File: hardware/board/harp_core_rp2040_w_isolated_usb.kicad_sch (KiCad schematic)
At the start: 49 parts, among them J1 Conn_01x03_Male, J2 AudioJack3, J3 USB_C_Receptacle_USB2.0, U2 TPD2EUSB30, U3 ADUM4160, U4 RP2040, U5 W25Q16JVUXIQ, X1 ECS-TXO-2016

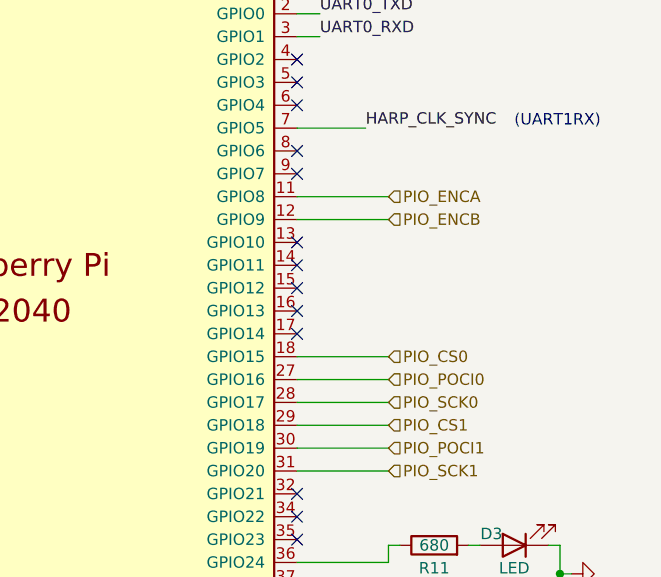
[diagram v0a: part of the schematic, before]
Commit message: update schematic
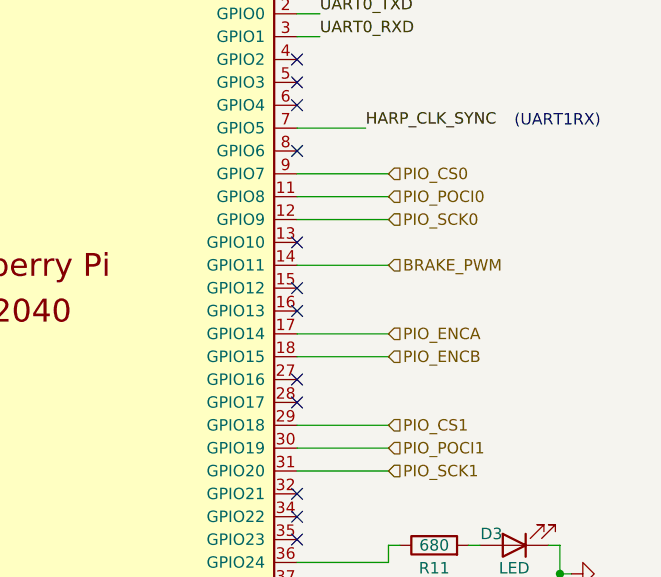
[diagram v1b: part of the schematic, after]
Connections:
- net PIO_CS0: now also U4.9 (GPIO7); no longer U4.18 (GPIO15)
- net PIO_ENCA: now also U4.17 (GPIO14); no longer U4.11 (GPIO8)
- net PIO_ENCB: now also U4.18 (GPIO15); no longer U4.12 (GPIO9)
- net PIO_POCI0: now also U4.11 (GPIO8); no longer U4.27 (GPIO16)
- net PIO_SCK0: now also U4.12 (GPIO9); no longer U4.28 (GPIO17)
- net BRAKE_PWM: now reaches U4.14 (GPIO11)
- no-connect marks 25 -> 24
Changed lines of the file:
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@@
   )
   (no_connect (at 244.475 144.78))
-  (no_connect (at 244.475 109.22))
   (no_connect (at 244.475 78.74))
-  (no_connect (at 244.475 101.6))
   (no_connect (at 244.475 147.32))
   (no_connect (at 244.475 132.08))
   (no_connect (at 244.475 81.28))
+  (no_connect (at 244.475 114.3))
   (no_connect (at 244.475 104.14))
   (no_connect (at 180.975 140.97))
@@
   (no_connect (at 180.975 114.3))
   (no_connect (at 244.475 83.82))
-  (no_connect (at 244.475 91.44))
   (no_connect (at 244.475 88.9))
   (no_connect (at 244.475 142.24))
+  (no_connect (at 244.475 99.06))
   (no_connect (at 244.475 106.68))
   (no_connect (at 42.545 52.07))
   (no_connect (at 29.845 105.41))
   (no_connect (at 139.065 109.22))
-  (no_connect (at 244.475 99.06))
+  (no_connect (at 244.475 116.84))
   (no_connect (at 244.475 149.86))
   (no_connect (at 244.475 129.54))
@@
     (stroke (width 0) (type default))
   )
-  (wire (pts (xy 244.475 111.76) (xy 254.635 111.76))
+  (wire (pts (xy 47.625 143.51) (xy 47.625 144.78))
     (stroke (width 0) (type default))
   )
-  (wire (pts (xy 47.625 143.51) (xy 47.625 144.78))
+  (wire (pts (xy 244.475 109.22) (xy 254.635 109.22))
     (stroke (width 0) (type default))
   )
@@
     (stroke (width 0) (type default))
   )
+  (wire (pts (xy 244.475 101.6) (xy 254.635 101.6))
+    (stroke (width 0) (type default))
+  )
   (wire (pts (xy 180.975 83.82) (xy 177.165 83.82))
     (stroke (width 0) (type default))
@@
     (stroke (width 0) (type default))
   )
-  (wire (pts (xy 244.475 114.3) (xy 254.635 114.3))
-    (stroke (width 0) (type default))
-  )
   (wire (pts (xy 244.475 119.38) (xy 254.635 119.38))
     (stroke (width 0) (type default))
@@
     (stroke (width 0) (type default))
   )
-  (wire (pts (xy 244.475 96.52) (xy 254.635 96.52))
+  (wire (pts (xy 244.475 93.98) (xy 254.635 93.98))
     (stroke (width 0) (type default))
   )
@@
     (stroke (width 0) (type default))
   )
-  (wire (pts (xy 244.475 93.98) (xy 254.635 93.98))
+  (wire (pts (xy 244.475 91.44) (xy 254.635 91.44))
     (stroke (width 0) (type default))
   )
@@
     (stroke (width 0) (type default))
   )
-  (wire (pts (xy 244.475 116.84) (xy 254.635 116.84))
-    (stroke (width 0) (type default))
-  )
   (wire (pts (xy 19.685 62.23) (xy 19.685 63.5))
     (stroke (width 0) (type default))
@@
     (stroke (width 0) (type default))
   )
+  (wire (pts (xy 244.475 111.76) (xy 254.635 111.76))
+    (stroke (width 0) (type default))
+  )
   (wire (pts (xy 19.685 63.5) (xy 27.305 63.5))
     (stroke (width 0) (type default))
@@
     (stroke (width 0) (type default))
   )
+  (wire (pts (xy 244.475 96.52) (xy 254.635 96.52))
+    (stroke (width 0) (type default))
+  )
   (wire (pts (xy 160.655 44.45) (xy 161.925 44.45))
     (stroke (width 0) (type default))
@@
     (effects (font (size 1.27 1.27)) (justify left))
   )
-  (hierarchical_label "PIO_POCI0" (shape input) (at 254.635 114.3 0) (fields_autoplaced)
+  (hierarchical_label "BRAKE_PWM" (shape input) (at 254.635 101.6 0) (fields_autoplaced)
+    (effects (font (size 1.27 1.27)) (justify left))
+  )
+  (hierarchical_label "PIO_POCI0" (shape input) (at 254.635 93.98 0) (fields_autoplaced)
     (effects (font (size 1.27 1.27)) (justify left))
   )
-  (hierarchical_label "PIO_SCK0" (shape input) (at 254.635 116.84 0) (fields_autoplaced)
+  (hierarchical_label "PIO_SCK0" (shape input) (at 254.635 96.52 0) (fields_autoplaced)
     (effects (font (size 1.27 1.27)) (justify left))
   )
-  (hierarchical_label "PIO_ENCA" (shape input) (at 254.635 93.98 0) (fields_autoplaced)
+  (hierarchical_label "PIO_ENCA" (shape input) (at 254.635 109.22 0) (fields_autoplaced)
     (effects (font (size 1.27 1.27)) (justify left))
   )
-  (hierarchical_label "PIO_ENCB" (shape input) (at 254.635 96.52 0) (fields_autoplaced)
+  (hierarchical_label "PIO_ENCB" (shape input) (at 254.635 111.76 0) (fields_autoplaced)
     (effects (font (size 1.27 1.27)) (justify left))
   )
-  (hierarchical_label "PIO_CS0" (shape input) (at 254.635 111.76 0) (fields_autoplaced)
+  (hierarchical_label "PIO_CS0" (shape input) (at 254.635 91.44 0) (fields_autoplaced)
     (effects (font (size 1.27 1.27)) (justify left))
   )

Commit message: update pcb
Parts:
- renumbered C2 to C1, C16 to C10, C17 to C11, C18 to C12, C19 to C13, C20 to C14, C21 to C15, C22 to C16, C23 to C17, C24 to C18, C25 to C19, C9 to C2, C11 to C3, C7 to C37, C8 to C4, C13 to C5, C5 to C56, C10 to C6, C12 to C7, C15 to C8, C14 to C9, D3 to D1, D4 to D2, D1 to D3, D2 to D4, J3 to J5, R9 to R10, R10 to R11, R8 to R9

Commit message: update sch and pcb
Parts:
- C11: Alternate CL21B106KOQNNNE -> GRM21BR61H106KE43L; Link https://www.digikey.com/en/products/detail/murata-electronics/GRM21BZ71E106KE15L/13904911 -> https://www.digikey.com/en/products/detail/murata-electronics/GRM21BR61H106KE43L/10326316; Manufacturer Number GRM21BZ71E106KE15L -> GRM21BR61H106KE43L; Rated Voltage 25V -> 50V; Temperature Coefficient X7R -> X5R; Tolerance (none) -> 10%
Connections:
- net BRAKE_PWM: now also U4.16 (GPIO13); no longer U4.14 (GPIO11)
- net PIO_CS0: now also U4.12 (GPIO9); no longer U4.9 (GPIO7)
- net PIO_ENCA: now also U4.27 (GPIO16); no longer U4.17 (GPIO14)
- net PIO_ENCB: now also U4.28 (GPIO17); no longer U4.18 (GPIO15)
- net PIO_POCI0: now also U4.13 (GPIO10); no longer U4.11 (GPIO8)
- net PIO_SCK0: now also U4.14 (GPIO11); no longer U4.12 (GPIO9)
- no-connect marks 24 -> 20

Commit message: update schematic; continue pcb draft
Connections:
- net BRAKE_PWM: now also U4.35 (GPIO23); no longer U4.16 (GPIO13)
- no-connect marks 20 -> 19
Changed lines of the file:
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@@
   (no_connect (at 244.602 78.74))
   (no_connect (at 244.602 147.32))
-  (no_connect (at 244.602 132.08))
   (no_connect (at 244.602 81.28))
   (no_connect (at 244.602 104.14))
@@
     (stroke (width 0) (type default))
   )
+  (wire (pts (xy 250.698 132.08) (xy 250.698 128.016))
+    (stroke (width 0) (type default))
+  )
   (wire (pts (xy 24.892 106.68) (xy 24.892 107.95))
     (stroke (width 0) (type default))
@@
     (stroke (width 0) (type default))
   )
-  (wire (pts (xy 244.602 106.68) (xy 254.762 106.68))
+  (wire (pts (xy 250.698 128.016) (xy 254.762 128.016))
     (stroke (width 0) (type default))
   )
@@
     (stroke (width 0) (type default))
   )
+  (wire (pts (xy 244.602 132.08) (xy 250.698 132.08))
+    (stroke (width 0) (type default))
+  )
   (wire (pts (xy 149.352 44.45) (xy 153.162 44.45))
     (stroke (width 0) (type default))
@@
     (effects (font (size 1.27 1.27)) (justify left))
   )
-  (hierarchical_label "BRAKE_PWM" (shape input) (at 254.762 106.68 0) (fields_autoplaced)
+  (hierarchical_label "BRAKE_PWM" (shape input) (at 254.762 128.016 0) (fields_autoplaced)
     (effects (font (size 1.27 1.27)) (justify left))
   )

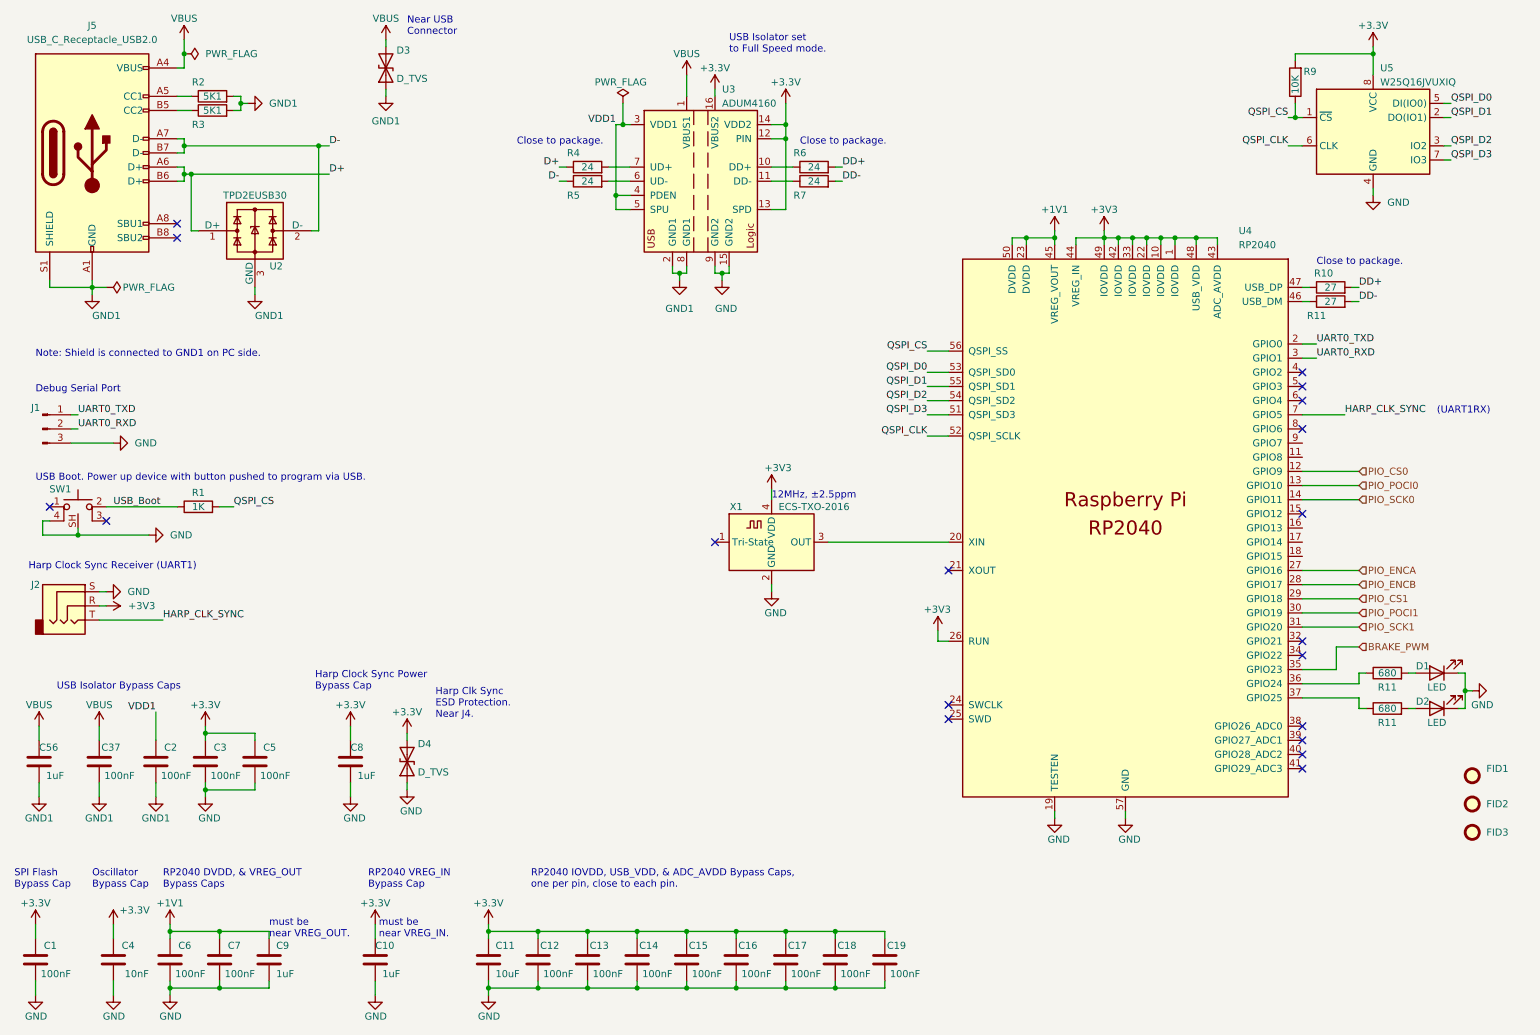
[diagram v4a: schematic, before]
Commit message: draft layout with analog brake driver circuit
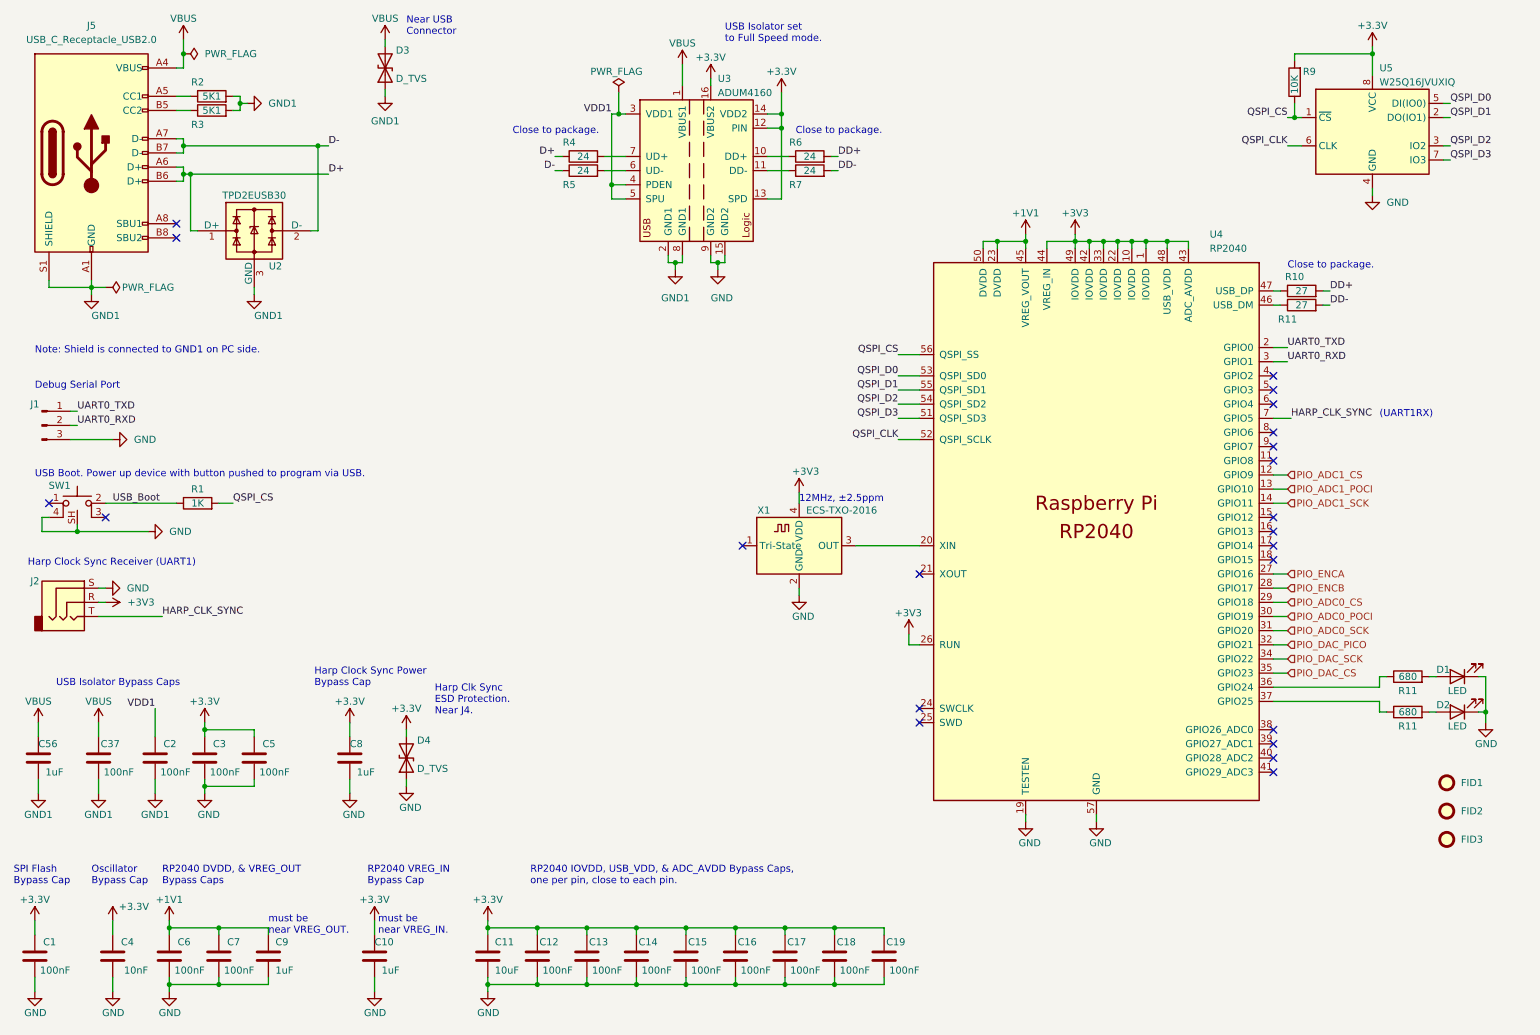
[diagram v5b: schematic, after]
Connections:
- net PIO_DAC_PICO: now reaches U4.32 (GPIO21)
- net PIO_DAC_SCK: now reaches U4.34 (GPIO22)
- net BRAKE_PWM renamed PIO_DAC_CS
- net PIO_CS0 renamed PIO_ADC1_CS
- net PIO_CS1 renamed PIO_ADC0_CS
- net PIO_POCI0 renamed PIO_ADC1_POCI
- net PIO_POCI1 renamed PIO_ADC0_POCI
- net PIO_SCK0 renamed PIO_ADC1_SCK
- net PIO_SCK1 renamed PIO_ADC0_SCK
- no-connect marks 19 -> 22
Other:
- moved on the sheet: C1, C10, C11, C12, C13, C14, C15, C16, C17, C18, C19, C2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

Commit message: draft v0.1 pcb
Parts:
- C4: Link https://www.digikey.com/en/products/detail/yageo/CC0402KPX7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 -> https://www.digikey.com/en/products/detail/murata-electroni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; Manufacturer Yageo -> Murata Electronics; Manufacturer Number CC0402KPX7R8BB103 -> GRM1555C1E103GE01D; Temperature Coefficient X7R -> COG/NP0; Tolerance 10% -> 2%; Vendor Number (none) -> 490-GRM1555C1E103GE01DDKR-ND
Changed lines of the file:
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@@
       (effects (font (size 1.27 1.27)) hide)
     )
-    (property "Datasheet" "https://www.yageo.com/upload/media/product/productsearch/datasheet/mlcc/UPY-GPHC_X7R_6.3V-to-250V_23.pdf" (at 31.115 183.515 0)
+    (property "Datasheet" "https://search.murata.co.jp/Ceramy/image/img/A01X/G101/ENG/GRM1555C1E103GE01-01A.pdf" (at 31.115 183.515 0)
       (effects (font (size 1.27 1.27)) hide)
     )
-    (property "Link" "https://www.digikey.com/en/products/detail/yageo/CC0402KPX7R8BB103/11490384" (at 31.115 183.515 0)
+    (property "Link" "https://www.digikey.com/en/products/detail/murata-electronics/GRM1555C1E103GE01D/16033920" (at 31.115 183.515 0)
       (effects (font (size 1.27 1.27)) hide)
     )
-    (property "Manufacturer" "Yageo" (at 31.115 183.515 0)
+    (property "Manufacturer" "Murata Electronics" (at 31.115 183.515 0)
       (effects (font (size 1.27 1.27)) hide)
     )
-    (property "Manufacturer Number" "CC0402KPX7R8BB103" (at 31.115 183.515 0)
+    (property "Manufacturer Number" "GRM1555C1E103GE01D" (at 31.115 183.515 0)
       (effects (font (size 1.27 1.27)) hide)
     )
@@
       (effects (font (size 1.27 1.27)) hide)
     )
-    (property "Temperature Coefficient" "X7R" (at 31.115 183.515 0)
+    (property "Temperature Coefficient" "COG/NP0" (at 31.115 183.515 0)
       (effects (font (size 1.27 1.27)) hide)
     )
-    (property "Tolerance" "10%" (at 31.115 183.515 0)
+    (property "Tolerance" "2%" (at 31.115 183.515 0)
       (effects (font (size 1.27 1.27)) hide)
     )
+    (property "Vendor Number" "490-GRM1555C1E103GE01DDKR-ND" (at 31.115 183.515 0)
+      (effects (font (size 1.27 1.27)) hide)
+    )

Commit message: draft firmware
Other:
- note added: "Note: PIO code as written assumes DAC CS_PIN is SCK_PIN + 1."
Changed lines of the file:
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@@
+    (effects (font (size 1.27 1.27)) (justify left bottom))
+  )
+  (text "Note:\nPIO code as written\nassumes DAC CS_PIN\nis SCK_PIN + 1."
+    (at 261.62 126.365 0)
     (effects (font (size 1.27 1.27)) (justify left bottom))
   )

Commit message: update pcb to v0.2.0
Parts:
- J2: Alternate SJ-3523-SMT-TR -> (none); Link https://www.digikey.com/en/products/detail/cui-devices/SJ-3524-SMT-TR-BE/2295987 -> https://www.digikey.com/en/products/detail/cui-devices/SJ-3523-SMT-TR/281297; Manufacturer Number SJ-3524-SMT-TR-BE -> SJ-3523-SMT-TR
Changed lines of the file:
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@@
       (effects (font (size 1.27 1.27)) hide)
     )
-    (property "Link" "https://www.digikey.com/en/products/detail/cui-devices/SJ-3524-SMT-TR-BE/2295987" (at 23.495 120.015 0)
+    (property "Link" "https://www.digikey.com/en/products/detail/cui-devices/SJ-3523-SMT-TR/281297" (at 23.495 120.015 0)
       (effects (font (size 1.27 1.27)) hide)
     )
@@
       (effects (font (size 1.27 1.27)) hide)
     )
-    (property "Manufacturer Number" "SJ-3524-SMT-TR-BE" (at 23.495 120.015 0)
+    (property "Manufacturer Number" "SJ-3523-SMT-TR" (at 23.495 120.015 0)
       (effects (font (size 1.27 1.27)) hide)
     )
-    (property "Alternate" "SJ-3523-SMT-TR" (at 23.495 120.015 0)
-      (effects (font (size 1.27 1.27)) hide)
-    )
